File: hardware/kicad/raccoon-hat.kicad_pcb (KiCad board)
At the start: 2 copper layers, 65 x 56 mm, 5 parts, among them J1 2x20_GPIO

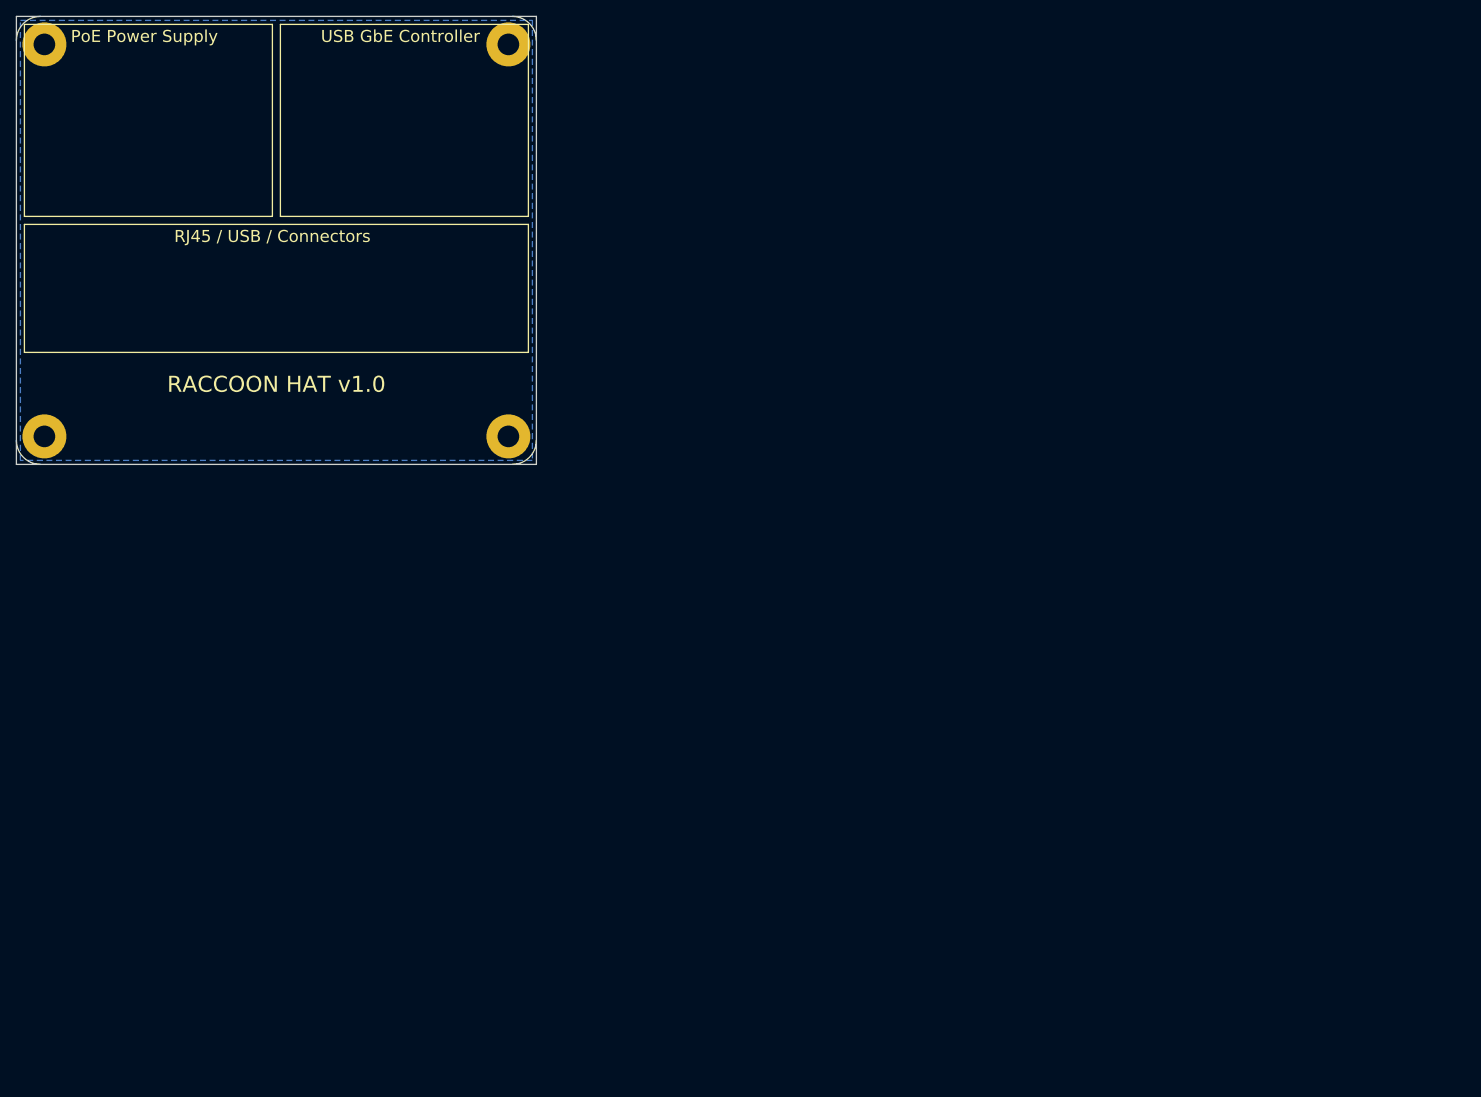
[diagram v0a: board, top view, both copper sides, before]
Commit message: Add functional PCB design, KiCad screenshots, and comprehensive hardware test suite
- Rewrite PCB with proper footprints, pads, traces, and copper zones (KiCad 10 format)
- Add matching schematic with all PoE + USB-to-GbE components
- Add PCB layout screenshot and 3D render to README
- Add 12 hardware tests covering full deployment lifecycle:
  smoke, throughput, power, continuity, bridge transparency,
  cover identity, NAC bypass, OPSEC scan, C2 beacon,
  sniffer/capture, SSH tunnel, and first-boot validation

Co-Authored-By: Claude Opus 4.6 <noreply@anthropic.com>
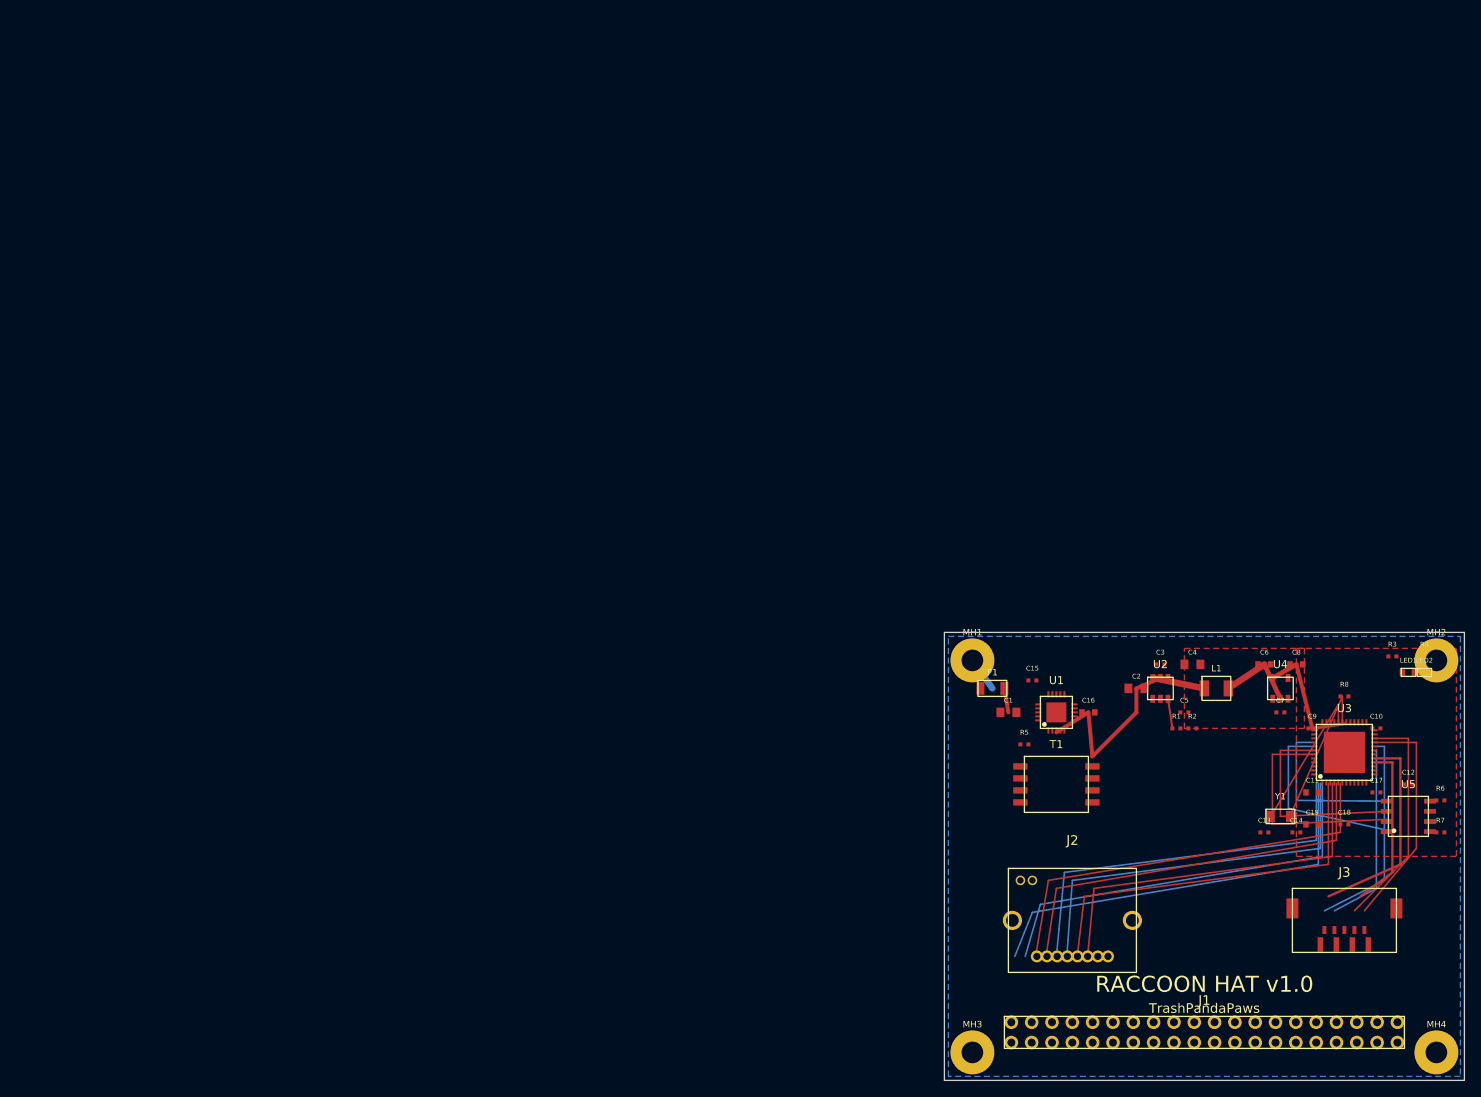
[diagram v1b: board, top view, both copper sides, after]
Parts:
- removed ? (x4): , MountingHole:MountingHole_2.7mm_M2.5_Pad_Via
- added C1: 100uF 63V, C_0805, F.Cu at (124.0, 87.0)
- added C10: 100nF, C_0402, F.Cu at (170.0, 89.0)
- added C11: 10uF, C_0603, F.Cu at (162.0, 97.0)
- added C12: 100nF, C_0402, F.Cu at (174.0, 96.0)
- added C13: 15pF, C_0402, F.Cu at (156.0, 102.0)
- added C14: 15pF, C_0402, F.Cu at (160.0, 102.0)
- added C15: 100nF, C_0402, F.Cu at (127.0, 83.0)
- added C16: 4.7uF, C_0603, F.Cu at (134.0, 87.0)
- added C17: 100nF, C_0402, F.Cu at (170.0, 97.0)
- added C18: 100nF DVDD12, C_0402, F.Cu at (166.0, 101.0)
- added C19: 10uF DVDD12, C_0603, F.Cu at (162.0, 101.0)
- added C2: 10uF 25V, C_0805, F.Cu at (140.0, 84.0)
- added C3: 100nF, C_0402, F.Cu at (143.0, 81.0)
- added C4: 22uF 10V, C_0805, F.Cu at (147.0, 81.0)
- added C5: 100nF BOOT, C_0402, F.Cu at (146.0, 87.0)
- added C6: 10uF, C_0603, F.Cu at (156.0, 81.0)
- added C7: 100nF, C_0402, F.Cu at (158.0, 87.0)
- added C8: 10uF, C_0603, F.Cu at (160.0, 81.0)
- added C9: 100nF, C_0402, F.Cu at (162.0, 89.0)
- added F1: 500mA, PTC_1206, F.Cu at (122.0, 84.0)
- added J2: HR911105A, RJ45_HR911105A, F.Cu at (132.0, 113.0)
- added J3: USB-A 3.0, USB-A_3.0_SMD, F.Cu at (166.0, 113.0)
- added L1: 10uH, Inductor_1210, F.Cu at (150.0, 84.0)
- added LED1: Green, LED_0603, F.Cu at (174.0, 82.0)
- added LED2: Amber, LED_0603, F.Cu at (176.0, 82.0)
- added MH1: MH, MountingHole_2.7mm_M2.5, F.Cu at (119.5, 80.5)
- added MH2: MH, MountingHole_2.7mm_M2.5, F.Cu at (177.5, 80.5)
- added MH3: MH, MountingHole_2.7mm_M2.5, F.Cu at (119.5, 129.5)
- added MH4: MH, MountingHole_2.7mm_M2.5, F.Cu at (177.5, 129.5)
- added R1: 24.9k, R_0402, F.Cu at (145.0, 89.0)
- added R2: 5.36k, R_0402, F.Cu at (147.0, 89.0)
- added R3: 330R, R_0402, F.Cu at (172.0, 80.0)
- added R4: 330R, R_0402, F.Cu at (176.0, 80.0)
- added R5: 25.5k, R_0402, F.Cu at (126.0, 91.0)
- added R6: 10k, R_0402, F.Cu at (178.0, 98.0)
- added R7: 10k, R_0402, F.Cu at (178.0, 102.0)
- added R8: 10k RST, R_0402, F.Cu at (166.0, 85.0)
- added T1: 750342460, Transformer_T1, F.Cu at (130.0, 96.0)
- added U1: SI3402-B, QFN-20_U1, F.Cu at (130.0, 87.0)
- added U2: TPS54302, SOT-23-6_U2, F.Cu at (143.0, 84.0)
- added U3: RTL8153B, QFN-48_U3, F.Cu at (166.0, 92.0)
- added U4: AP2112K-3.3, SOT-23-5_U4, F.Cu at (158.0, 84.0)
- added U5: W25Q16, SOIC-8_U5, F.Cu at (174.0, 100.0)
- added Y1: 25MHz, Crystal_3215, F.Cu at (158.0, 100.0)
- J1: value 2x20_GPIO -> 2x20 GPIO; footprint Connector_PinHeader_2.54mm:PinHeader_2x20_P2.54mm_Vertical -> PinHeader_2x20_P2.54mm
- moved J1 139.5 mm to (148.5, 127.0)
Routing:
- net ETH_MDI2P: track 0.00 -> 52.8 mm
- net ETH_MDI3N: track 0.00 -> 52.3 mm
- net ETH_MDI3P: track 0.00 -> 51.7 mm
- net ETH_MDI2N: track 0.00 -> 51.3 mm
- net ETH_MDI1N: track 0.00 -> 49.5 mm
- net ETH_MDI1P: track 0.00 -> 48.9 mm
- net ETH_MDI0N: track 0.00 -> 48.5 mm
- net ETH_MDI0P: track 0.00 -> 47.8 mm
- net USB_SSTXP: track 0.00 -> 28.6 mm
- net USB_SSTXN: track 0.00 -> 28.5 mm
- net SPI_MOSI: track 0.00 -> 28.2 mm
- net USB_SSRXN: track 0.00 -> 26.3 mm
- net USB_DM: track 0.00 -> 26.2 mm
- net SPI_MISO: track 0.00 -> 25.7 mm
- net +12V: track 0.00 -> 24.3 mm
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- added copper zone on F.Cu, net +3V3
- added copper zone on F.Cu, net +5V
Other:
- outline, holes or cut-outs redrawn
- board text added: "PoE Ethernet Tap — RPi 4"
- board text added: "TrashPandaPaws"
- board text removed: "PoE Ethernet Tap — Raspberry Pi 4"
- board text removed: "PoE Power Supply"
- board text removed: "RJ45 / USB / Connectors"
- board text removed: "USB GbE Controller"
